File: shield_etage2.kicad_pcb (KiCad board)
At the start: 2 copper layers, 70 parts, among them J1 Conn_01x02, J10 ToF, J11 Moteur, J12 Moteur, J13 butee, J14 butee, J15 Pixy, J16 comm_f3, J17 Moteur, J18 butee, J19 Conn_01x02, J2 Conn_01x02, J3 ToF, J4 ToF, J5 ToF, J6 ToF, J7 ToF, J8 ToF, J9 ToF, Q1 BSS138, Q2 BSS138, Q3 BSS138, Q4 BSS138, Q5 BSS138, Q6 BSS138, Q7 BSS138, SW1 SW_Push, U1 74HC164, U2 LM317_TO3, U3 LM317_TO3, U4 LM317_TO3, U5 L293D, U6 L293D

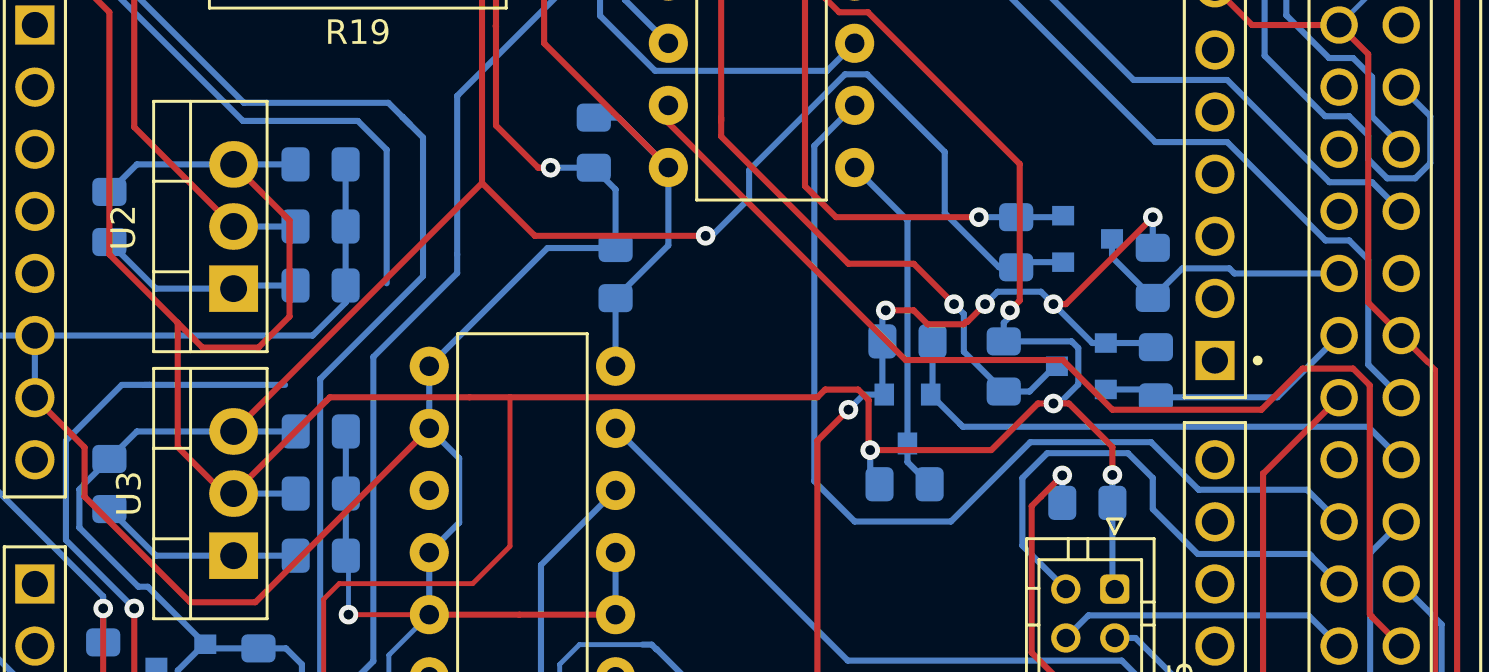
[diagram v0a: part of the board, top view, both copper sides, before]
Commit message: addition of second motor and ArUco outputs, note the last edition is the one called gange
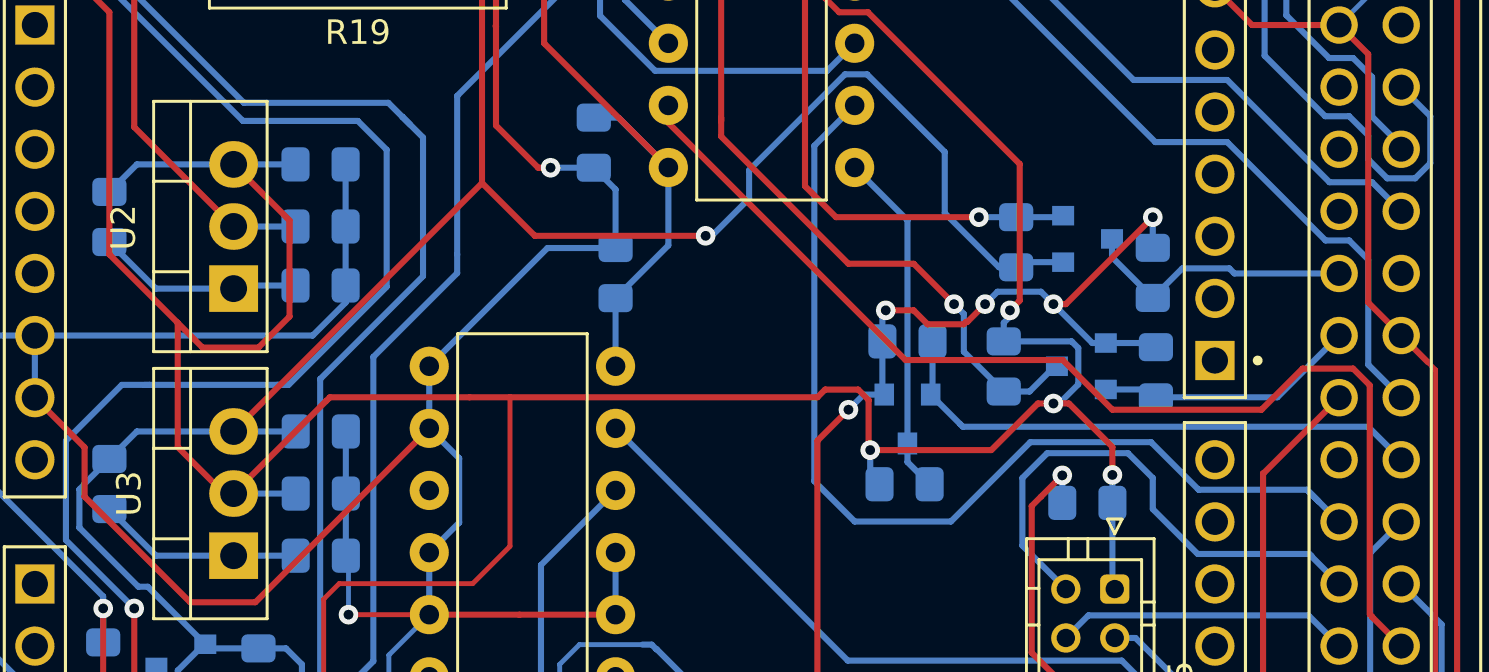
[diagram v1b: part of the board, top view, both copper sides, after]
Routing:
- net /LevelShifter_ShiftRegister/ShiftRegister_DSAB: track 69.7 -> 76.0 mm
- net /Driver_moteurs/bras2_sens_direct: track 40.9 -> 41.6 mm

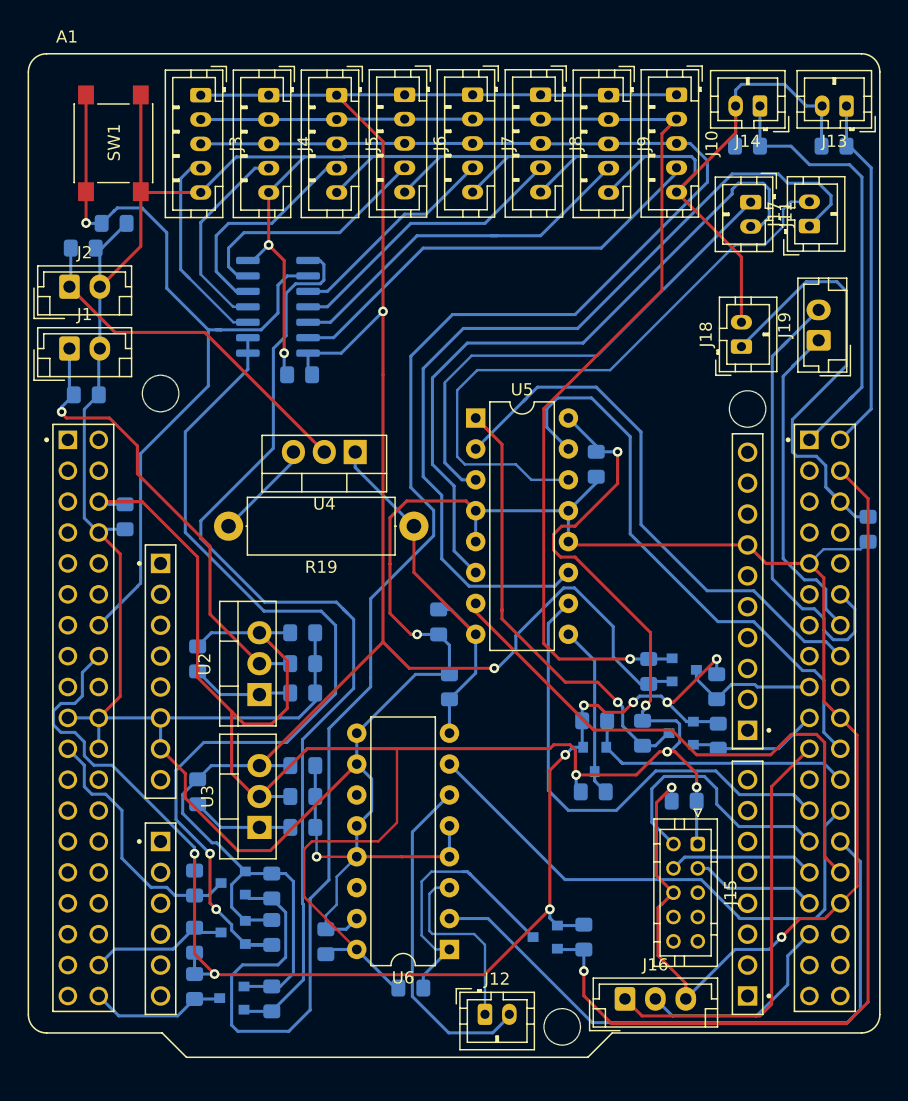
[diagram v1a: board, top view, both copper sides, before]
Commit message: removed psi-things pins, added transceiver MCP2551 for CAN, changed motors input protocol, RS must be chosen 1 or 10 kohms, and a foot print for a potentitial 120 ohms resistor is present for CAN bus end.
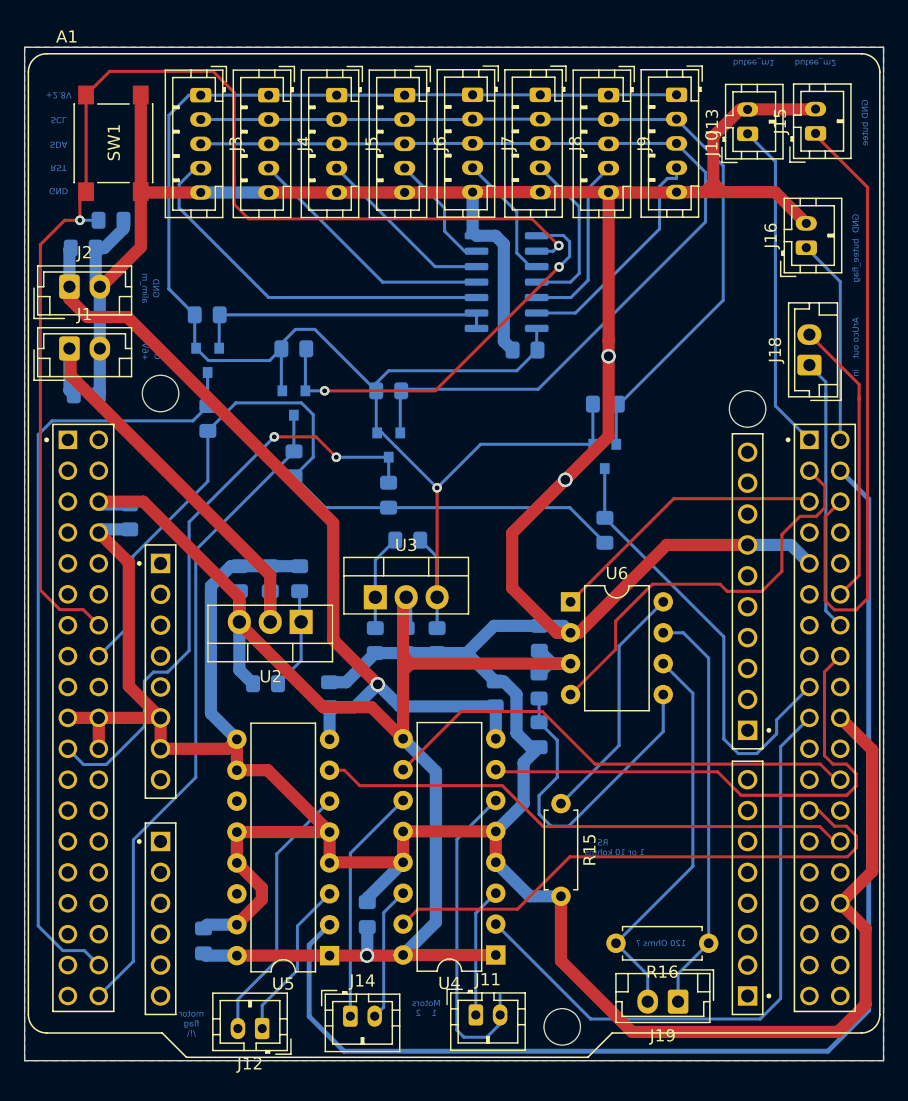
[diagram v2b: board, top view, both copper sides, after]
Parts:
- removed C15: 1µ, Capacitor_SMD:C_0805_2012Metric_Pad1.15x1.40mm_HandSolder
- removed C16, C17: 100n, Capacitor_SMD:C_0805_2012Metric_Pad1.15x1.40mm_HandSolder
- removed J17: Moteur, Connector_JST:JST_PH_B2B-PH-K_1x02_P2.00mm_Vertical
- removed Q5, Q6, Q7: BSS138, Package_TO_SOT_SMD:SOT-23
- removed R17, R18: Pull, Resistor_SMD:R_0805_2012Metric_Pad1.15x1.40mm_HandSolder
- removed R19: 1.2, Resistor_THT:R_Axial_DIN0414_L11.9mm_D4.5mm_P15.24mm_Horizontal
- C12: value 100n -> 1µ
- J14: value butee -> Moteur
- J15: value Pixy -> butee; footprint Connector_JST:JST_PHD_B10B-PHDSS_2x05_P2.00mm_Vertical -> Connector_JST:JST_PH_B2B-PH-K_1x02_P2.00mm_Vertical
- J16: value comm_f3 -> butee; footprint Connector_JST:JST_EH_B3B-EH-A_1x03_P2.50mm_Vertical -> Connector_JST:JST_PH_B2B-PH-K_1x02_P2.00mm_Vertical
- J18: value butee -> Conn_01x02; footprint Connector_JST:JST_PH_B2B-PH-K_1x02_P2.00mm_Vertical -> Connector_JST:JST_EH_B2B-EH-A_1x02_P2.50mm_Vertical
- J19: value Conn_01x02 -> output_CAN
- R13, R14: value Pull -> 470
- R15: value Pull -> 10k; footprint Resistor_SMD:R_0805_2012Metric_Pad1.15x1.40mm_HandSolder -> Resistor_THT:R_Axial_DIN0207_L6.3mm_D2.5mm_P7.62mm_Horizontal; moved to F.Cu
- R16: value Pull -> 120; footprint Resistor_SMD:R_0805_2012Metric_Pad1.15x1.40mm_HandSolder -> Resistor_THT:R_Axial_DIN0207_L6.3mm_D2.5mm_P7.62mm_Horizontal; moved to F.Cu
- U4: value LM317_TO3 -> L293D; footprint Package_TO_SOT_THT:TO-220-3_Vertical -> Package_DIP:DIP-16_W7.62mm
- U6: value L293D -> MCP2551-I-P; footprint Package_DIP:DIP-16_W7.62mm -> Package_DIP:DIP-8_W7.62mm
- moved J14 82.1 mm to (95.4, 149.8), turned to 0 degrees
- moved J11 70.5 mm to (105.7, 149.7), turned to 0 degrees
- moved C12 65.4 mm to (77.2, 108.7), turned to 270 degrees
- moved J16 63.5 mm to (132.8, 86.6), turned to 90 degrees
- moved J15 59.2 mm to (133.6, 77.2), turned to 90 degrees
- moved J19 55.6 mm to (122.3, 148.6), turned to 180 degrees
- moved R6 53.5 mm to (90.7, 94.9), turned to 0 degrees
- moved C13 52.7 mm to (75.7, 84.3), turned to 0 degrees
- moved R5 51.1 mm to (83.6, 92.1), turned to 0 degrees
- moved Q4 49.2 mm to (90.7, 99.3), turned to 270 degrees
- moved Q3 47.1 mm to (83.6, 95.8), turned to 270 degrees
- moved U5 45.8 mm to (93.6, 144.8), turned to 180 degrees
- moved R8 43.7 mm to (90.7, 104.4), turned to 90 degrees
- moved U4 42.9 mm to (107.3, 144.7)
- moved R7 42.9 mm to (83.6, 100.6)
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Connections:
- A1 pad CN10_12: /ArU.sch/ArUco2 -> /ArUco.sch/ArUco2
- A1 pad CN10_14: /ArU.sch/ArUco1 -> /ArUco.sch/ArUco1
- A1 pad CN10_16: /Driver_moteurs/bras1_sens_direct -> /Driver_moteurs/sens_bras1
- A1 pad CN10_19: /F4/bras1_PWM -> /Driver_moteurs/pwm_bras1
- A1 pad CN10_21: /UART_comm_f3/TX -> (no net)
- A1 pad CN10_22: /Driver_moteurs/bras2_sens_inverse -> (no net)
- A1 pad CN10_24: /F4/bras2_PWM -> /Driver_moteurs/pwm_bras2
- A1 pad CN10_25: /Driver_moteurs/bras2_sens_direct -> /Driver_moteurs/sens_bras2
- A1 pad CN10_26: /Driver_moteurs/drapeau_sens_inverse -> (no net)
- A1 pad CN10_27: /pixy/SPI_MISO -> (no net)
- A1 pad CN10_28: /Driver_moteurs/drapeau_sens_direct -> /Driver_moteurs/sens_drapeau
- A1 pad CN10_29: /pixy/SPI_CLK -> (no net)
- A1 pad CN10_3: (no net) -> /F4/CAN1_RX
- A1 pad CN10_30: /Driver_moteurs/bras1_sens_inverse -> (no net)
- A1 pad CN10_31: /pixy/SPI_MOSI -> (no net)
- A1 pad CN10_33: /UART_comm_f3/RX -> (no net)
- A1 pad CN10_4: /F4/drapeau_PWM -> /Driver_moteurs/pwm_drapeau
- A1 pad CN10_5: (no net) -> /F4/CAN1_TX
- C11 pad 2: Net-(C11-Pad2) -> ALIM_MOTEURS
- C12 pad 1: /FinDeCourse_drapeau/STM32_GPIO -> +5V
- C13 pad 1: /FinDeCourse_bras1/STM32_GPIO -> /F4/NRST
- C14 pad 1: +5V -> GND
- C14 pad 2: GND -> +5V
- C9 pad 2: Net-(C11-Pad2) -> ALIM_MOTEURS
- J13 pad 1: /FinDeCourse_drapeau/STM32_GPIO -> /FinDeCourse_bras1/STM32_GPIO
- J14 pad 1: /FinDeCourse_bras1/STM32_GPIO -> /Driver_moteurs/moteur2_pin1
- J14 pad 2: GND -> /Driver_moteurs/moteur2_pin2
- J15 pad 1: +5V -> /FinDeCourse_bras2/STM32_GPIO
- J15 pad 2: /pixy/SPI_MISO -> GND
- J16 pad 1: /UART_comm_f3/TX -> /FinDeCourse_drapeau/STM32_GPIO
- J16 pad 2: /UART_comm_f3/RX -> GND
- J18 pad 1: /FinDeCourse_bras2/STM32_GPIO -> /ArUco.sch/ArUco1
- J18 pad 2: GND -> /ArUco.sch/ArUco2
- J19 pad 1: /ArU.sch/ArUco1 -> Net-(J19-Pad1)
- J19 pad 2: /ArU.sch/ArUco2 -> Net-(J19-Pad2)
- R13 pad 1: +3V3 -> Net-(R13-Pad1)
- R13 pad 2: /F4/bras1_PWM -> +5V
- R14 pad 1: +3V3 -> GND
- R14 pad 2: /F4/bras2_PWM -> Net-(R13-Pad1)
- R15 pad 1: +3V3 -> Net-(R15-Pad1)
- R15 pad 2: /F4/drapeau_PWM -> GND
- R16 pad 1: +5V -> Net-(J19-Pad1)
- R16 pad 2: /Driver_moteurs/PWM_bras1 -> Net-(J19-Pad2)
- U4 pad 1: Net-(C11-Pad2) -> +5V
- U4 pad 2: ALIM_MOTEURS -> /Driver_moteurs/pwm_bras1
- U4 pad 3: Net-(R19-Pad2) -> /Driver_moteurs/moteur1_pin1
- U5 pad 1: /Driver_moteurs/PWM_bras1 -> +5V
- U5 pad 10: /Driver_moteurs/bras2_sens_direct -> GND
- U5 pad 11: /Driver_moteurs/moteur2_pin1 -> (no net)
- U5 pad 14: /Driver_moteurs/moteur2_pin2 -> (no net)
- U5 pad 15: /Driver_moteurs/bras2_sens_inverse -> GND
- U5 pad 2: /Driver_moteurs/bras1_sens_direct -> /Driver_moteurs/pwm_drapeau
- U5 pad 3: /Driver_moteurs/moteur1_pin1 -> /Driver_moteurs/moteur3_pin1
- U5 pad 6: /Driver_moteurs/moteur1_pin2 -> /Driver_moteurs/moteur3_pin2
- U5 pad 7: /Driver_moteurs/bras1_sens_inverse -> /Driver_moteurs/sens_drapeau
- U5 pad 8: Net-(C11-Pad2) -> ALIM_MOTEURS
- U5 pad 9: /Driver_moteurs/PWM_bras2 -> GND
- U6 pad 1: /Driver_moteurs/PWM_drapeau -> /F4/CAN1_TX
- U6 pad 2: /Driver_moteurs/drapeau_sens_direct -> GND
- U6 pad 3: /Driver_moteurs/moteur3_pin1 -> +5V
- U6 pad 4: GND -> /F4/CAN1_RX
- U6 pad 5: GND -> Net-(R13-Pad1)
- U6 pad 6: /Driver_moteurs/moteur3_pin2 -> Net-(J19-Pad2)
- U6 pad 7: /Driver_moteurs/drapeau_sens_inverse -> Net-(J19-Pad1)
- U6 pad 8: Net-(C11-Pad2) -> Net-(R15-Pad1)
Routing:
- net /Driver_moteurs/pwm_drapeau: track 0.00 -> 102.1 mm
- net /LevelShifter_ToF_I2C/I2C_SDA_ToF: track 157.2 -> 80.9 mm
- net /F4/drapeau_PWM: track 75.7 -> 0.00 mm, vias 1 -> 0
- net +5V: track 179.7 -> 126.1 mm, vias 5 -> 1
- net /Driver_moteurs/moteur2_pin1: track 72.2 -> 19.5 mm
- net /LevelShifter_ShiftRegister/STM32_DSAB: track 11.7 -> 64.4 mm
- net /Driver_moteurs/drapeau_sens_direct: track 52.6 -> 0.00 mm
- net /Driver_moteurs/pwm_bras1: track 0.00 -> 51.4 mm
- net /LevelShifter_ShiftRegister/ShiftRegister_DSAB: track 76.0 -> 25.2 mm, vias 2 -> 0
- net /LevelShifter_ShiftRegister/ShiftRegister_CP: track 82.5 -> 33.9 mm, vias 0 -> 2
- net /Driver_moteurs/bras2_sens_inverse: track 47.7 -> 0.00 mm
- net +3V3: track 112.3 -> 65.8 mm, vias 8 -> 0
- net /Driver_moteurs/bras1_sens_inverse: track 46.4 -> 0.00 mm
- net /Driver_moteurs/bras1_sens_direct: track 46.1 -> 0.00 mm
- net /Driver_moteurs/sens_bras2: track 0.00 -> 45.5 mm
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- added copper zone on B.Cu, net GND
- added copper zone on F.Cu, net GND
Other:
- board outline added: 70.6 x 83.3 mm
- net class Power  added: clearance 0.4, trace_width 1, via_dia 1.2, via_drill 0.8
- rule trace_min: 0.2 -> 0.249
- board text added: "+2.8V"
- board text added: "+6V"
- board text added: "120 Ohms ?"
- board text added: "ArUco out in"
- board text added: "CAN H - L"
- board text added: "GND"
- board text added: "Motors 1 2"
- board text added: "RS 1 or 10 kohms"
- board text added: "RST"
- board text added: "SCL"
- board text added: "SDA"
- board text added: "alim_m"
- board text added: "butee"
- board text added: "butee_flag"
- board text added: "butee_m1"
- board text added: "butee_m2"
- board text added: "motor flag /!\"

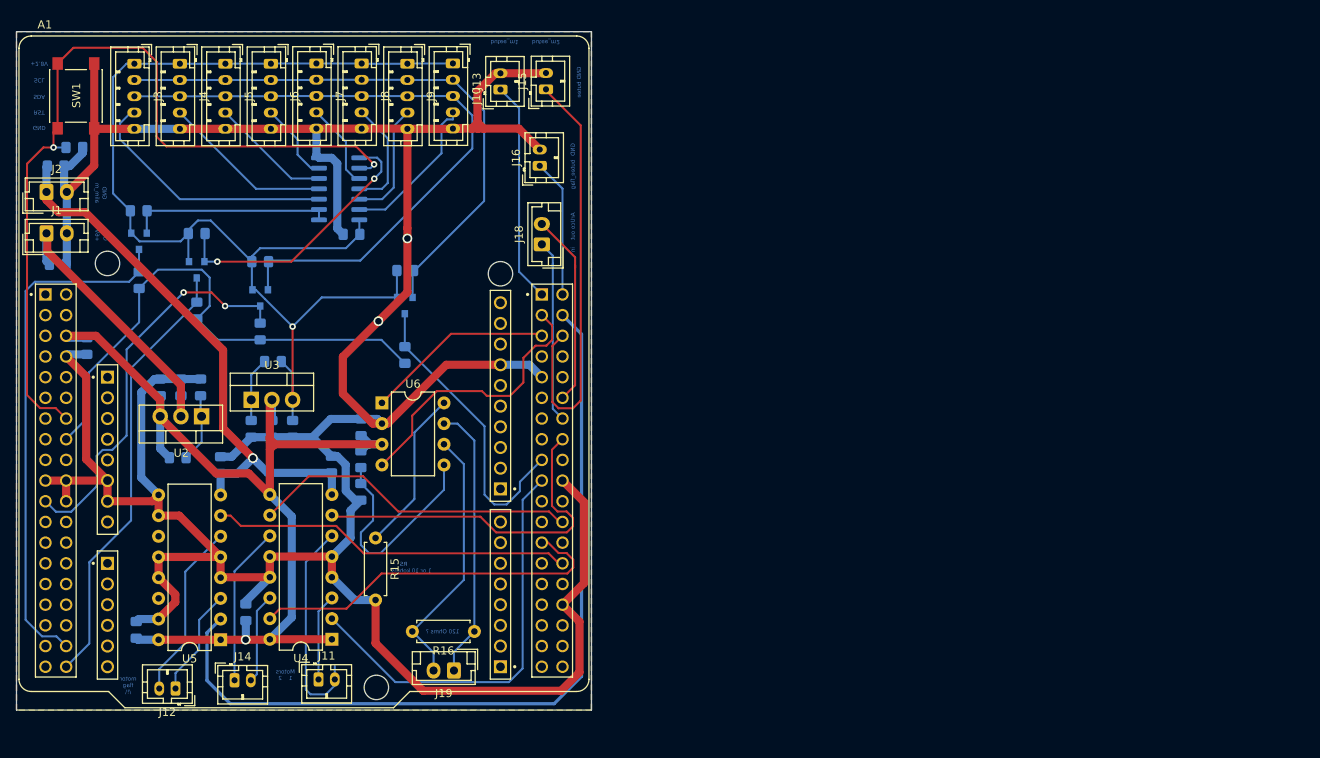
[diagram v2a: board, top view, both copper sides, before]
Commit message: oops, some component where on the wrong side....
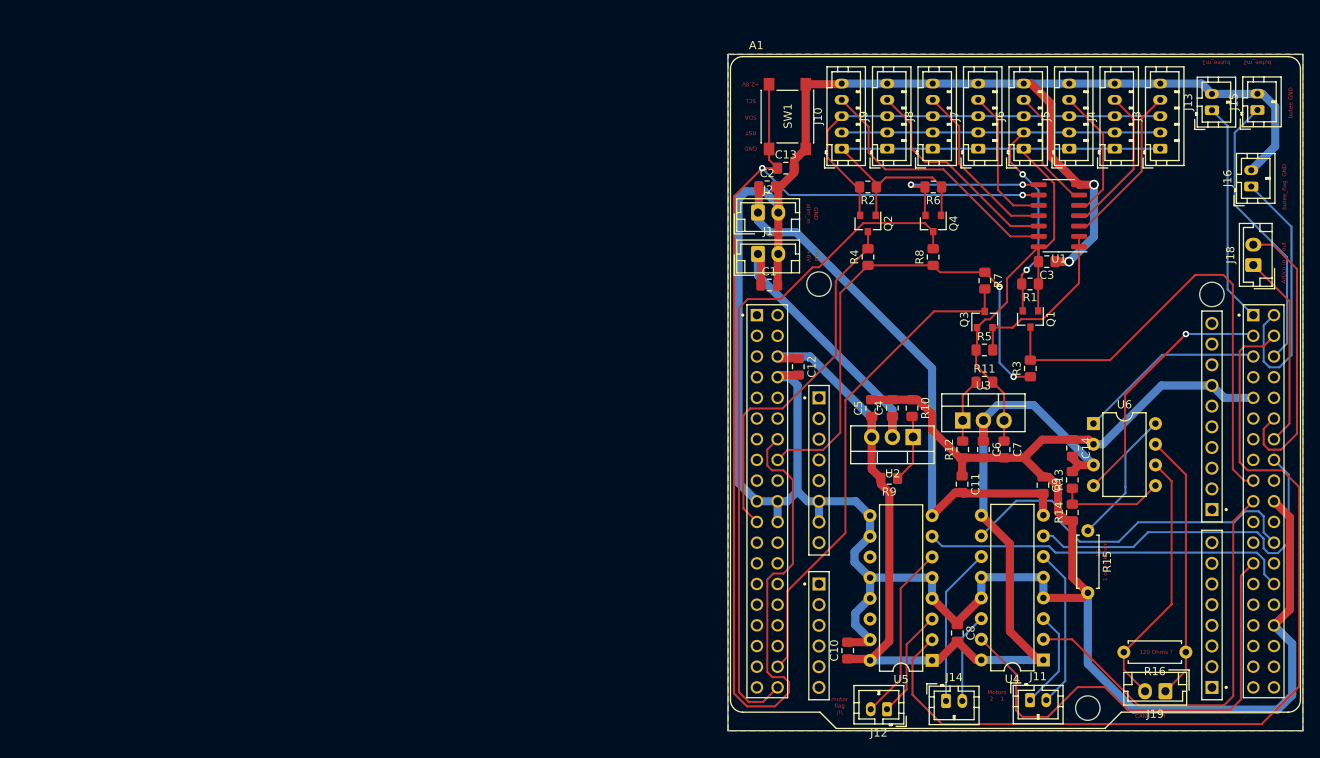
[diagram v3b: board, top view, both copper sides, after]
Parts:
- C1, C10, C11, C12, C13, C14, C2, C3, C4, C5, C6, C7, C8, C9, Q1, Q2, Q3, Q4, R1, R10, R11, R12, R13, R14, R2, R3, R4, R5, R6, R7, R8, R9, U1: moved to F.Cu
- moved J3 126.4 mm to (209.0, 84.5), turned to 90 degrees
- moved J4 115.3 mm to (203.5, 84.5), turned to 90 degrees
- moved R5 105.3 mm to (187.5, 109.2)
- moved Q3 104.3 mm to (187.5, 105.5), turned to 90 degrees
- moved J5 104.2 mm to (197.9, 84.5), turned to 90 degrees
- moved R7 103.9 mm to (187.5, 100.7), turned to 270 degrees
- moved J6 93.0 mm to (192.3, 84.5), turned to 90 degrees
- moved C11 91.1 mm to (184.7, 125.7)
- moved R8 90.7 mm to (181.2, 97.8)
- moved R6 90.6 mm to (181.2, 89.2), turned to 180 degrees
- moved Q4 90.6 mm to (181.2, 93.7)
- moved U1 88.5 mm to (196.6, 92.7), turned to 180 degrees
- moved R15 87.5 mm to (200.2, 131.4)
- moved C12 87.4 mm to (164.6, 111.3)
- moved J11 87.4 mm to (193.0, 152.2)
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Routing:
- net /F4/NRST: track 103.5 -> 159.8 mm
- net +2V8: track 146.2 -> 113.3 mm, vias 1 -> 0
- net /LevelShifter_ShiftRegister/STM32_CP: track 54.4 -> 83.9 mm
- net /LevelShifter_ToF_I2C/I2C_SDA_ToF: track 80.9 -> 53.9 mm
- net /LevelShifter_ToF_I2C/I2C_SCL_STM32: track 36.8 -> 59.5 mm
- net /FinDeCourse_bras2/STM32_GPIO: track 52.8 -> 34.8 mm
- net /FinDeCourse_drapeau/STM32_GPIO: track 17.0 -> 33.3 mm
- net Net-(R13-Pad1): track 27.6 -> 13.1 mm
- net /ShiftRegister/Reset_ToF_7: track 19.0 -> 33.0 mm
- net /Driver_moteurs/sens_bras2: track 45.5 -> 59.0 mm
- net /LevelShifter_ShiftRegister/ShiftRegister_CP: track 33.9 -> 21.0 mm
- net /ShiftRegister/Reset_ToF_6: track 14.7 -> 26.8 mm
- net /ArUco.sch/ArUco2: track 23.9 -> 35.7 mm
- net /ShiftRegister/Reset_ToF_0: track 31.8 -> 20.2 mm
- net +5V: track 126.1 -> 134.8 mm, vias 1 -> 0
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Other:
- board size 70.6 x 83.3 mm -> 70.6 x 83.1 mm
- board text added: "ArUco in out"
- board text added: "CAN L - H"
- board text added: "Motors 2 1"
- board text removed: "ArUco out in"
- board text removed: "CAN H - L"
- board text removed: "Motors 1 2"

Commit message: some tweaks after Xavier's review
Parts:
- moved R12 7.56 mm to (190.4, 116.3), turned to 270 degrees
- moved C7 6.85 mm to (185.3, 116.3), turned to 90 degrees
- moved U3 5.95 mm to (190.4, 119.9), turned to 180 degrees
- moved C6 5.12 mm to (187.8, 116.3), turned to 90 degrees
- turned R11 to 180 degrees
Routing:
- net /F4/NRST: track 159.8 -> 85.9 mm, vias 2 -> 3
- net GND: track 409.5 -> 423.5 mm
- net +5V: track 134.8 -> 128.5 mm
- net /Driver_moteurs/sens_bras2: track 59.0 -> 53.9 mm
- net Net-(R11-Pad1): track 7.92 -> 11.6 mm, vias 0 -> 1
- net +2V8: track 113.3 -> 114.1 mm
- removed copper zone on B.Cu, net GND
- removed copper zone on F.Cu, net GND
